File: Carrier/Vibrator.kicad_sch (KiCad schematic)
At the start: 5 parts, among them M1 Z30C1T8460001, Q4 BC847

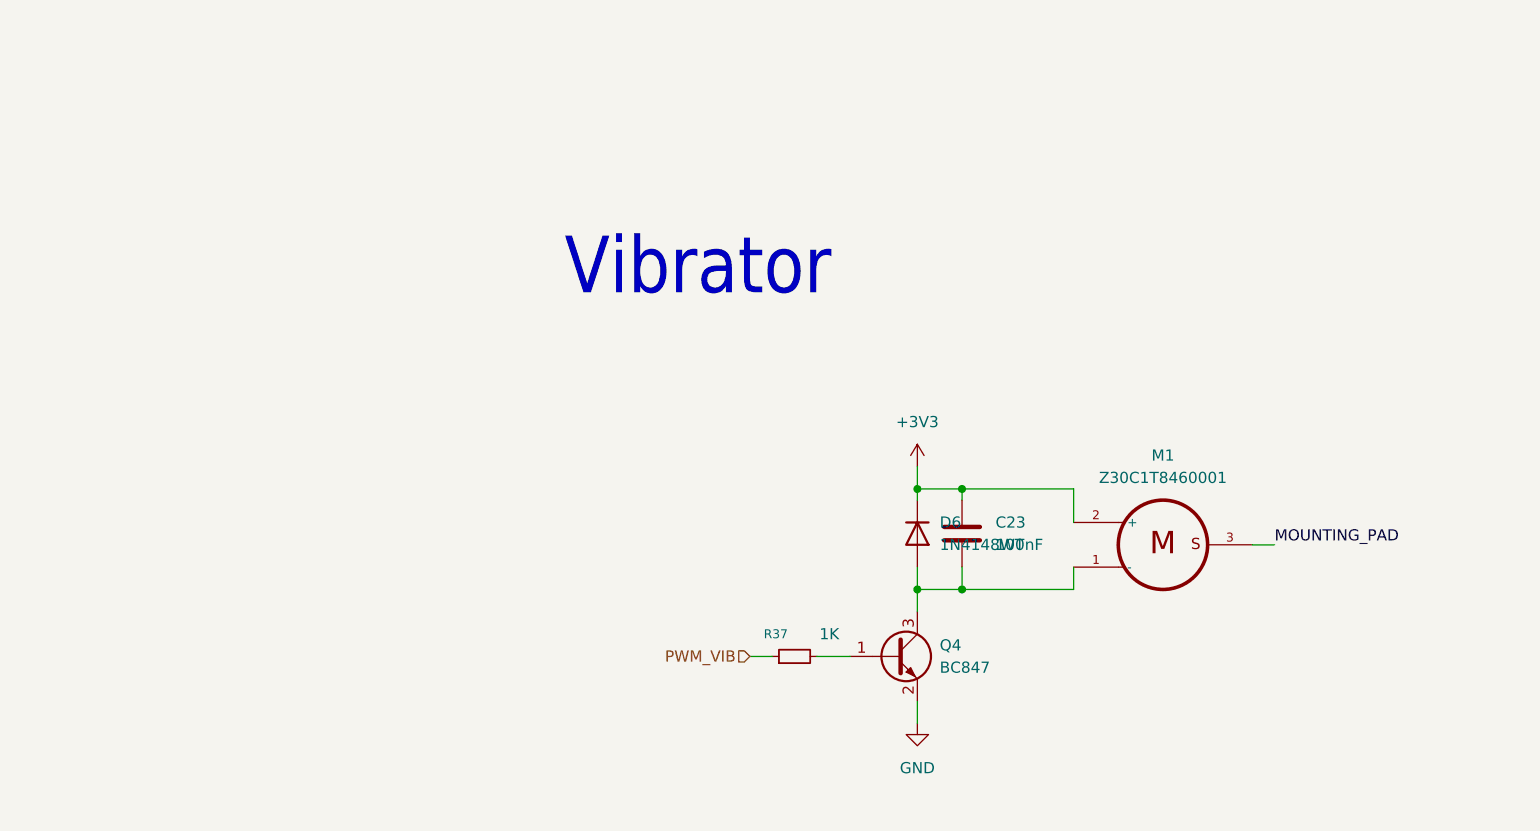
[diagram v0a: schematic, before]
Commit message: fix: add ordercodes for production files
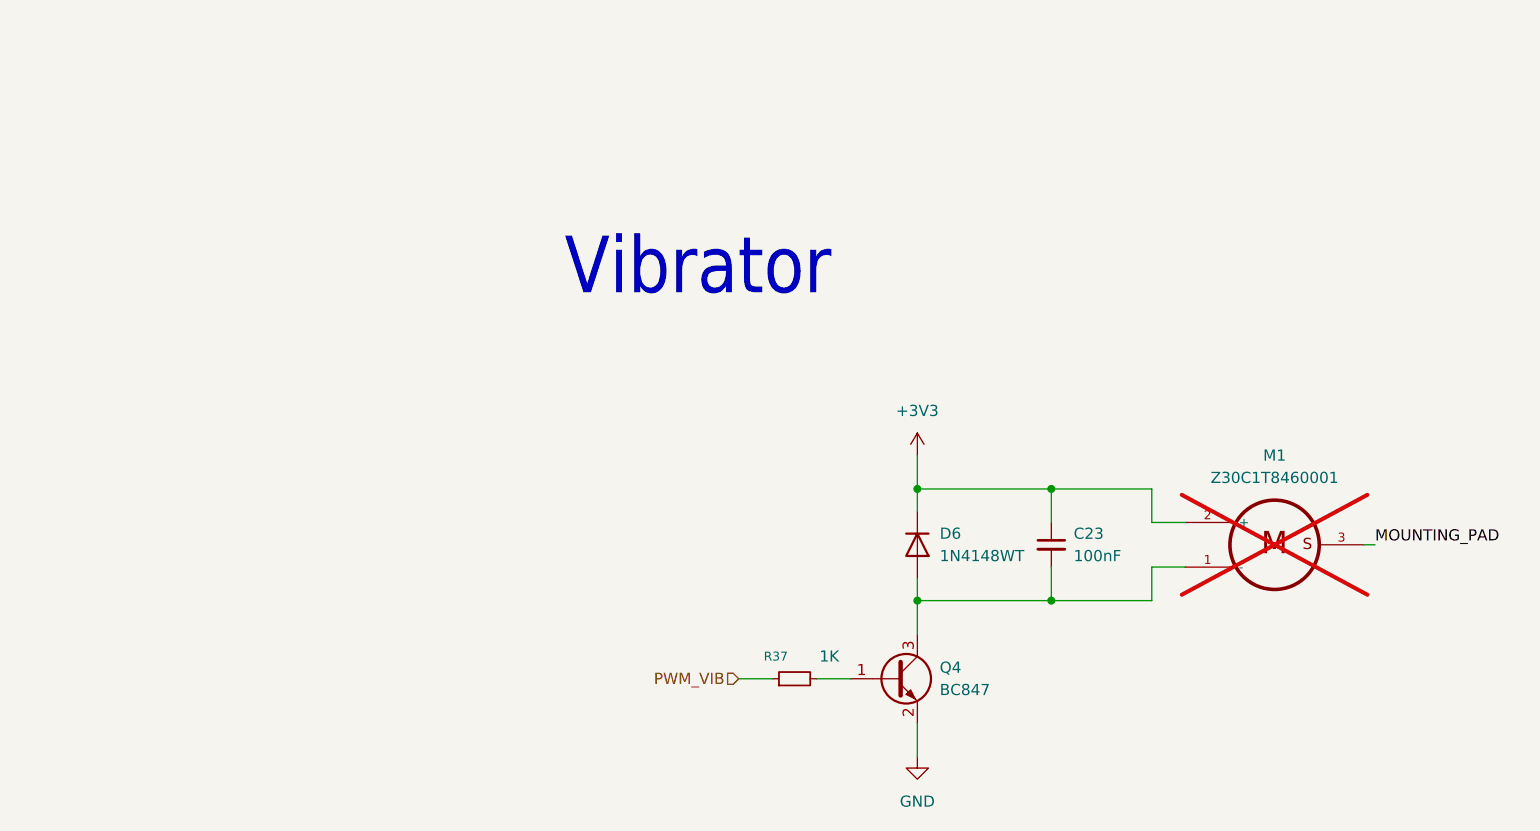
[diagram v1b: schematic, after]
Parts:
- removed C23: 100nF, Capacitor_SMD:C_0805_2012Metric, symbol Device:C
- added C23: 100nF, Capacitor_SMD:C_0402_1005Metric, symbol Device:C_Small
- D6: LCSC (none) -> C232841
- M1: now not fitted
- Q4: LCSC (none) -> C2926209
- R37: LCSC C25900 -> C11702
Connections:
- net +3V3: now also C23.1
- net at D6.2 (A), M1.1 (-), Q4.3 (C): now also C23.2
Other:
- moved on the sheet: D6, Q4, R37

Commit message: chore: lib cleanup
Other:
- moved on the sheet: C23, D6, M1, Q4, R37

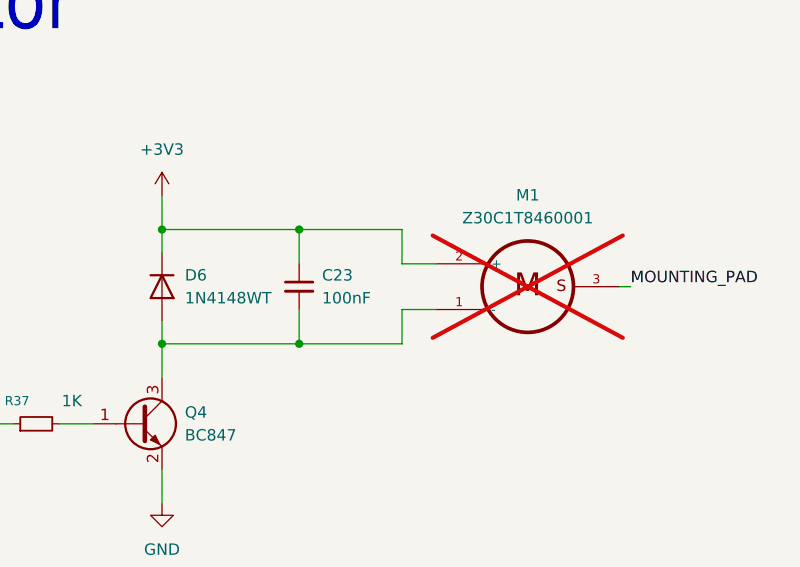
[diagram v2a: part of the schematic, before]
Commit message: STOCK LCSC vibr, and silkscreen changes
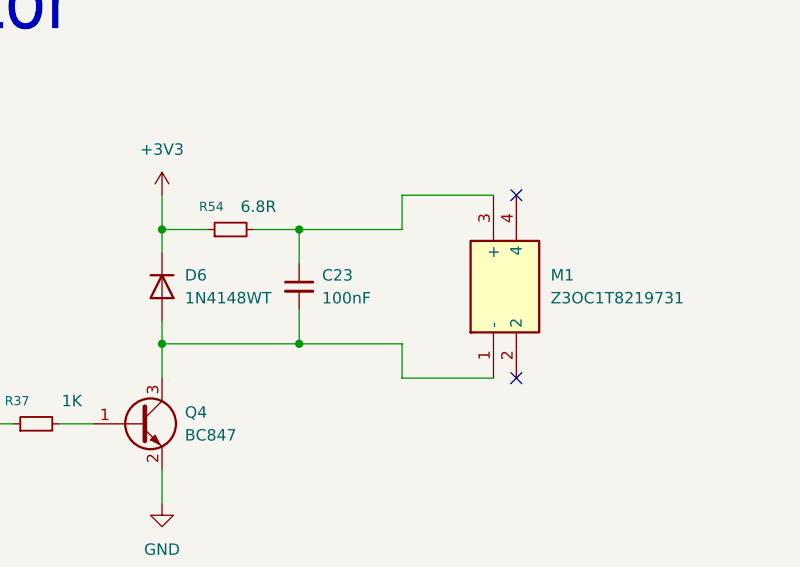
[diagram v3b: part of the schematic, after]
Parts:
- removed M1: Z30C1T8460001, Z30C1T8460001:XDCR_Z30C1T8460001, symbol Z30C1T8460001:Z30C1T8460001
- added M1: Z3OC1T8219731, Z3OC1T8219731, symbol Z3OC1T8219731:Z3OC1T8219731
- added R54: 6.8R, Resistor_SMD:R_0402_1005Metric, symbol Device:R_Small
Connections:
- net +3V3: now also R54.1; no longer C23.1
- net at C23.2, D6.2 (A), Q4.3 (C): now also M1.1 (-)
- new net: C23.1, M1.3 (+), R54.2
- no-connect marks 0 -> 2

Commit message: fix: drc errors & prod files
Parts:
- M1: LCSC (none) -> C2894731
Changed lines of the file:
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@@
+			)
+		)
+		(property "LCSC" "C2894731"
+			(at 109.22 77.47 90)
+			(effects
+				(font
+					(size 1.27 1.27)
+				)
+				(hide yes)
 			)
 		)

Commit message: Moved lcd screen connector for new screen, corrected LCSC partnumbers
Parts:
- R54: LCSC C11702 -> C38373
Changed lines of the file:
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@@
 			)
 		)
-		(property "LCSC" "C11702"
+		(property "LCSC" "C38373"
 			(at 80.01 60.96 0)
 			(effects
